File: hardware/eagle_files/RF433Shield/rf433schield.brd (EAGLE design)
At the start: 100 x 80 mm, 2 parts, among them U1 ARDUINOR3-DIMENSION

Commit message: New version
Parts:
- added U$2: ICEEPOT_LOGO, RFM:ICEEPOT_LOGO
- moved U$1 15.5 mm to (27.9, 15.2)
- moved U1 8.03 mm to (7.62, 2.54)
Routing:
- net N$2: track 48.6 -> 61.4 mm
- net N$4: track 0.00 -> 8.89 mm
- net N$3: track 56.1 -> 49.0 mm, vias 2 -> 0
- added copper zone on layer 16, net GND

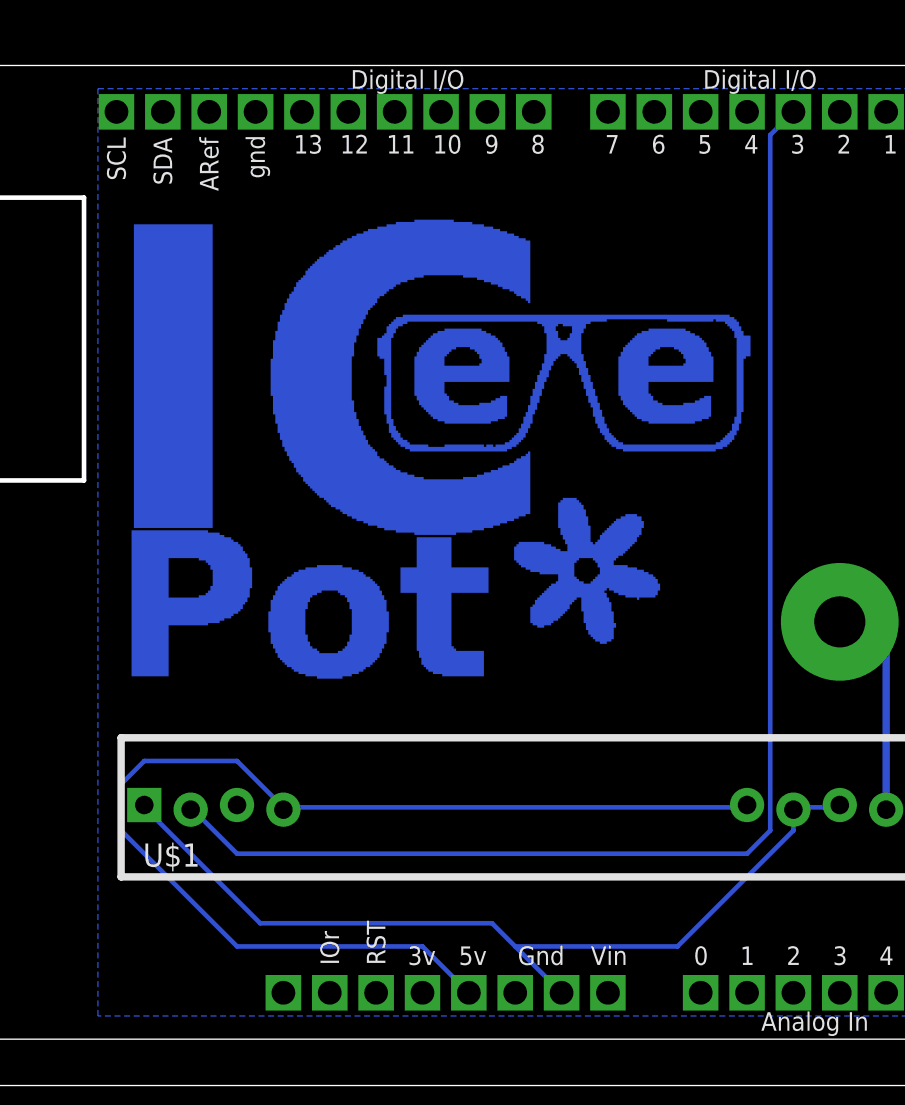
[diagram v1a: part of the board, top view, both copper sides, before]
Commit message: Added ICeePot logo on the copper of the board
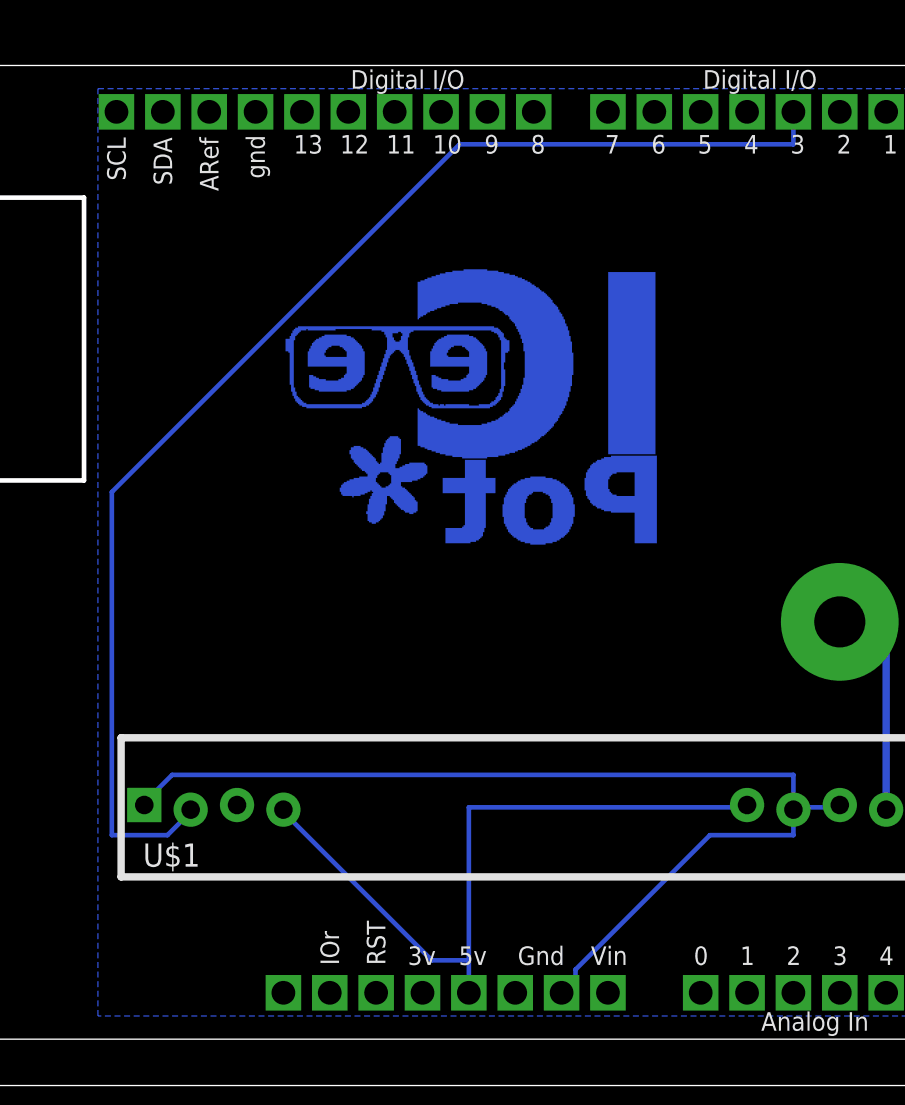
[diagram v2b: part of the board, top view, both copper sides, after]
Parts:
- removed U$2: ICEEPOT_LOGO, RFM:ICEEPOT_LOGO
- added E$1: (no value), RFM:ICEEPOT_LOGO_REV
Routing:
- net N$2: track 61.4 -> 39.2 mm
- net N$3: track 49.0 -> 58.9 mm
- net N$1: track 73.4 -> 70.8 mm
